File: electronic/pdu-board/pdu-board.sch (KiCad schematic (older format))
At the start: 28 parts, among them J1 Raspberry_D, J10 TERM, J11 SWITCH, J12 Raspberry_MGMT, J13 PWM_RPI, J14 FAN_B, J15 FAN_A, J2 Raspberry_C, J3 Raspberry_B, J4 Raspberry_A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

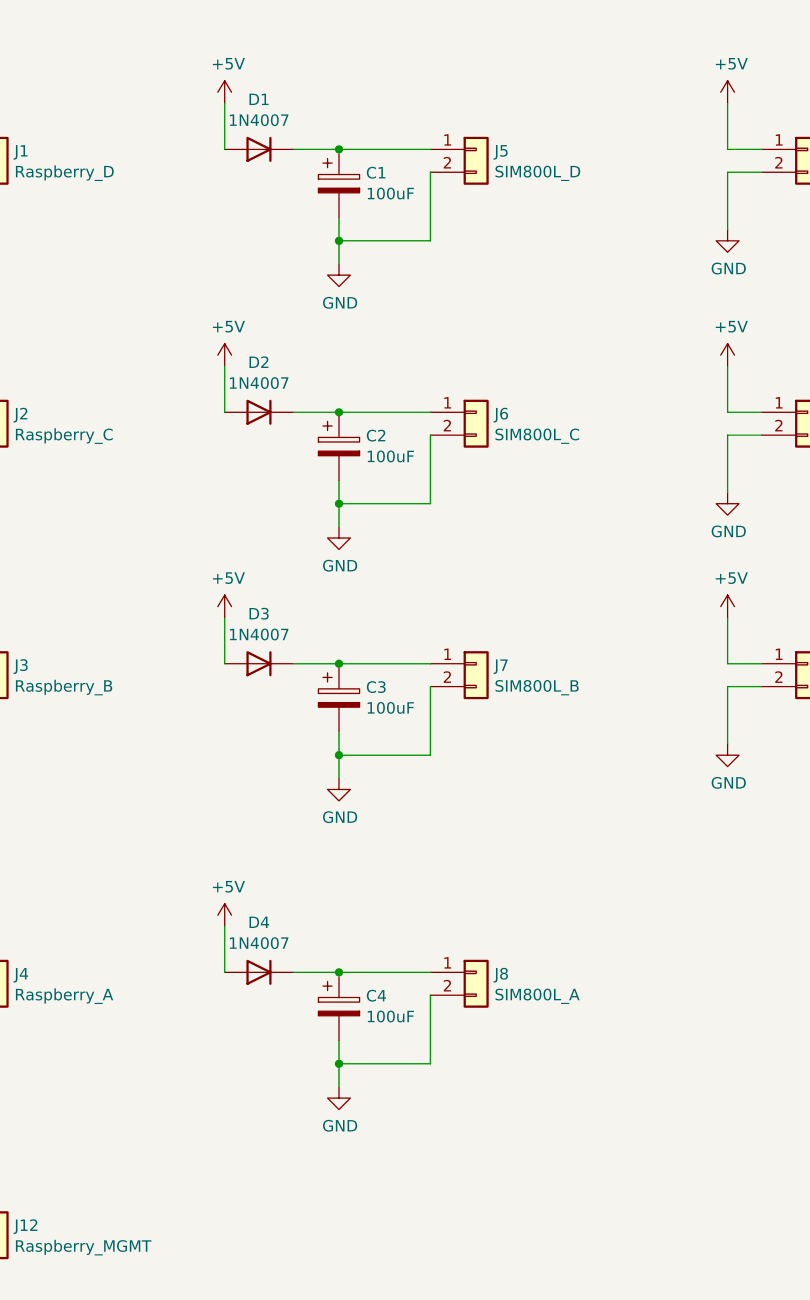
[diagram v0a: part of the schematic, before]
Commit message: RTC + GSM board
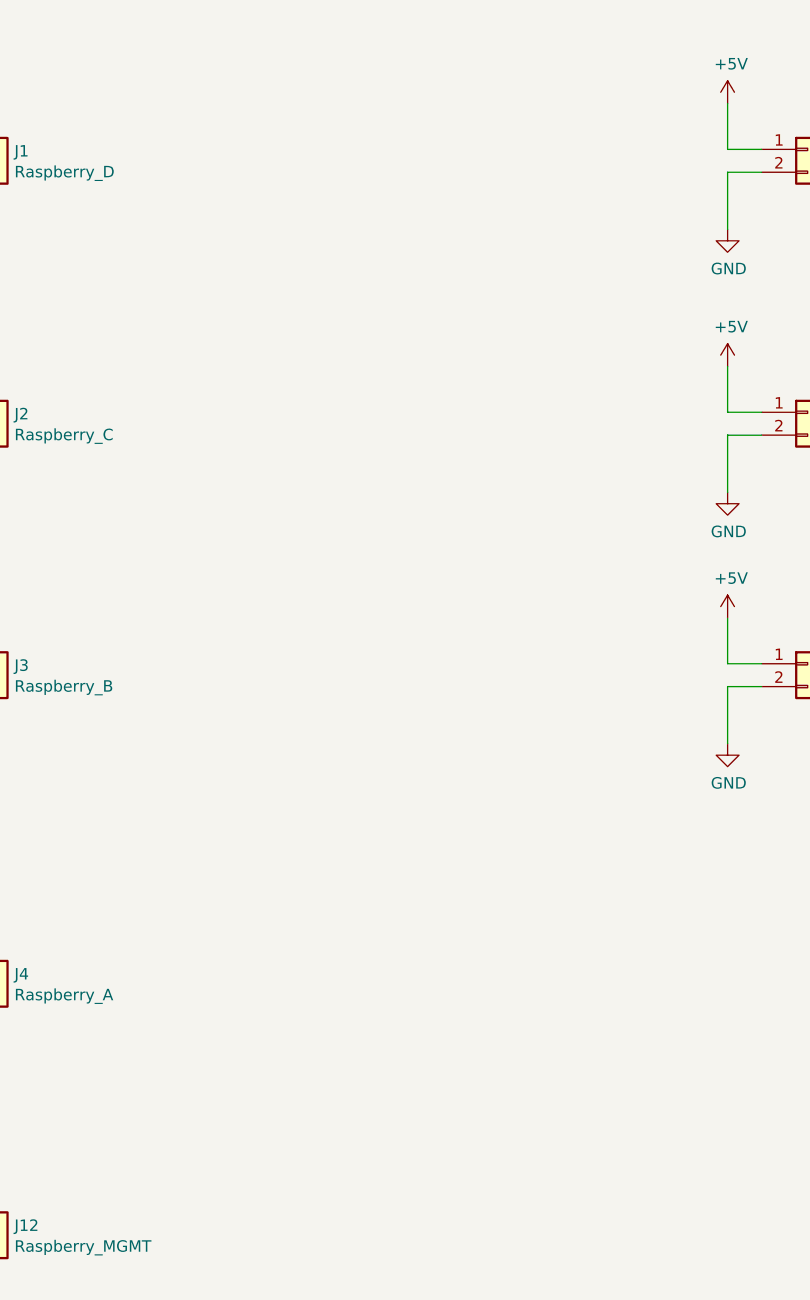
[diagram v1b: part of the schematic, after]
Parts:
- removed C1, C2, C3, C4: 100uF, Capacitor_THT:CP_Radial_D6.3mm_P2.50mm, symbol Device:CP
- removed D1, D2, D3, D4: 1N4007, Diode_THT:D_DO-41_SOD81_P10.16mm_Horizontal, symbol Diode:1N4007
- removed J5: SIM800L_D, TerminalBlock_Phoenix:TerminalBlock_Phoenix_MKDS-3-2-5.08_1x02_P5.08mm_Horizontal, symbol Connector_Generic:Conn_01x02
- removed J6: SIM800L_C, TerminalBlock_Phoenix:TerminalBlock_Phoenix_MKDS-3-2-5.08_1x02_P5.08mm_Horizontal, symbol Connector_Generic:Conn_01x02
- removed J7: SIM800L_B, TerminalBlock_Phoenix:TerminalBlock_Phoenix_MKDS-3-2-5.08_1x02_P5.08mm_Horizontal, symbol Connector_Generic:Conn_01x02
- removed J8: SIM800L_A, TerminalBlock_Phoenix:TerminalBlock_Phoenix_MKDS-3-2-5.08_1x02_P5.08mm_Horizontal, symbol Connector_Generic:Conn_01x02
